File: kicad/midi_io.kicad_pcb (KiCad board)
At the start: 2 copper layers, 35.6 x 41.4 mm, 10 parts, among them J1 MIDI Out, J2 MIDI In, J3 Conn_01x04, U1 6N138

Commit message: Possible final PCB layout
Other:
- net class Default: clearance 0.0508 -> 0.1524
- rule trace_clearance: 0.0508 -> 0.1524
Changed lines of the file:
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@@
     (thickness 1.6)
     (drawings 9)
-    (tracks 52)
+    (tracks 53)
     (zones 0)
     (modules 10)
@@
     (user_trace_width 0.508)
     (user_trace_width 0.762)
-    (trace_clearance 0.0508)
+    (trace_clearance 0.1524)
     (zone_clearance 0.508)
     (zone_45_only no)
@@
     (mod_text_size 1 1)
     (mod_text_width 0.15)
-    (pad_size 4.064 4.064)
-    (pad_drill 3.048)
+    (pad_size 1.7 1.7)
+    (pad_drill 1)
     (pad_to_mask_clearance 0.0508)
     (solder_mask_min_width 0.1016)
@@
   (net 17 "Net-(U1-Pad1)")
   (net_class Default "This is the default net class."
-    (clearance 0.0508)
+    (clearance 0.1524)
     (trace_width 0.254)
     (via_dia 0.508)
@@
   (module midi_io:CUI_SDS-50J (layer F.Cu)
     (at 123.952 94.869 270)
-    (fp_text reference J2 (at -9.144 -1.778 180) (layer F.SilkS)
+    (fp_text reference J2 (at -9.144 -1.778 180) (layer F.SilkS) hide
       (effects (font (size 1.0007 1.0007) (thickness 0.1524)))
     )
@@
   (module midi_io:CUI_SDS-50J (layer F.Cu)
     (at 123.952 115.443 270)
-    (fp_text reference J1 (at -9.398 -1.524 180) (layer F.SilkS)
+    (fp_text reference J1 (at -9.398 -1.524 180) (layer F.SilkS) hide
       (effects (font (size 1.0007 1.0007) (thickness 0.1524)))
     )
@@
     (descr "Through hole straight pin header, 1x04, 2.54mm pitch, single row")
     (tags "Through hole pin header THT 1x04 2.54mm single row")
-    (fp_text reference J3 (at -0.127 10.16) (layer F.SilkS)
+    (fp_text reference J3 (at -0.127 10.16) (layer F.SilkS) hide
       (effects (font (size 1 1) (thickness 0.15)))
     )
@@
     (pad 2 thru_hole oval (at 0 2.54) (size 1.7 1.7) (drill 1) (layers *.Cu *.Mask)
       (net 1 GND))
-    (pad 1 thru_hole rect (at 0 0) (size 1.7 1.7) (drill 1) (layers *.Cu *.Mask)
+    (pad 1 thru_hole circle (at 0 0) (size 1.7 1.7) (drill 1) (layers *.Cu *.Mask)
       (net 7 VCC))
     (model ${KISYS3DMOD}/Connector_PinHeader_2.54mm.3dshapes/PinHeader_1x04_P2.54mm_Vertical.wrl
@@
   (segment (start 131.064 92.583) (end 131.826 91.821) (width 0.254) (layer F.Cu) (net 6))
   (segment (start 144.018 111.633) (end 141.478 111.633) (width 0.508) (layer B.Cu) (net 7))
-  (via (at 134.366 120.523) (size 0.508) (drill 0.254) (layers F.Cu B.Cu) (net 7))
   (segment (start 134.366 120.523) (end 132.343 120.523) (width 0.508) (layer F.Cu) (net 7))
-  (segment (start 135.89 118.999) (end 134.366 120.523) (width 0.508) (layer B.Cu) (net 7))
-  (segment (start 135.89 114.173) (end 135.89 118.999) (width 0.508) (layer B.Cu) (net 7))
+  (segment (start 135.89 118.999) (end 135.89 118.999) (width 0.508) (layer F.Cu) (net 7))
   (segment (start 141.478 111.633) (end 138.43 111.633) (width 0.508) (layer B.Cu) (net 7))
   (segment (start 138.43 111.633) (end 135.89 114.173) (width 0.508) (layer B.Cu) (net 7))
@@
   (segment (start 141.487 103.242) (end 143.002 101.727) (width 0.254) (layer F.Cu) (net 7))
   (segment (start 141.487 105.791) (end 141.487 103.242) (width 0.254) (layer F.Cu) (net 7))
+  (segment (start 135.89 114.173) (end 135.89 118.999) (width 0.508) (layer B.Cu) (net 7))
+  (segment (start 135.89 118.999) (end 134.366 120.523) (width 0.508) (layer F.Cu) (net 7))
+  (via (at 135.89 118.999) (size 0.508) (drill 0.254) (layers F.Cu B.Cu) (net 7))
   (segment (start 139.7 119.253) (end 144.018 119.253) (width 0.254) (layer F.Cu) (net 8))
   (segment (start 137.414 116.967) (end 139.7 119.253) (width 0.254) (layer F.Cu) (net 8))

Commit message: Misc
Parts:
- moved R4 20.9 mm to (160.8, 100.7)
- moved D1 20.9 mm to (159.0, 83.4)
- moved J1 20.9 mm to (144.3, 110.4)
- moved J2 20.9 mm to (144.3, 89.8)
- moved J3 20.9 mm to (164.3, 106.6)
- moved R1 20.9 mm to (151.6, 115.4)
- moved R2 20.9 mm to (151.6, 105.3)
- moved R3 20.9 mm to (151.4, 90.8)
- moved R5 20.9 mm to (151.4, 95.1)
- moved U1 20.9 mm to (163.3, 89.0)

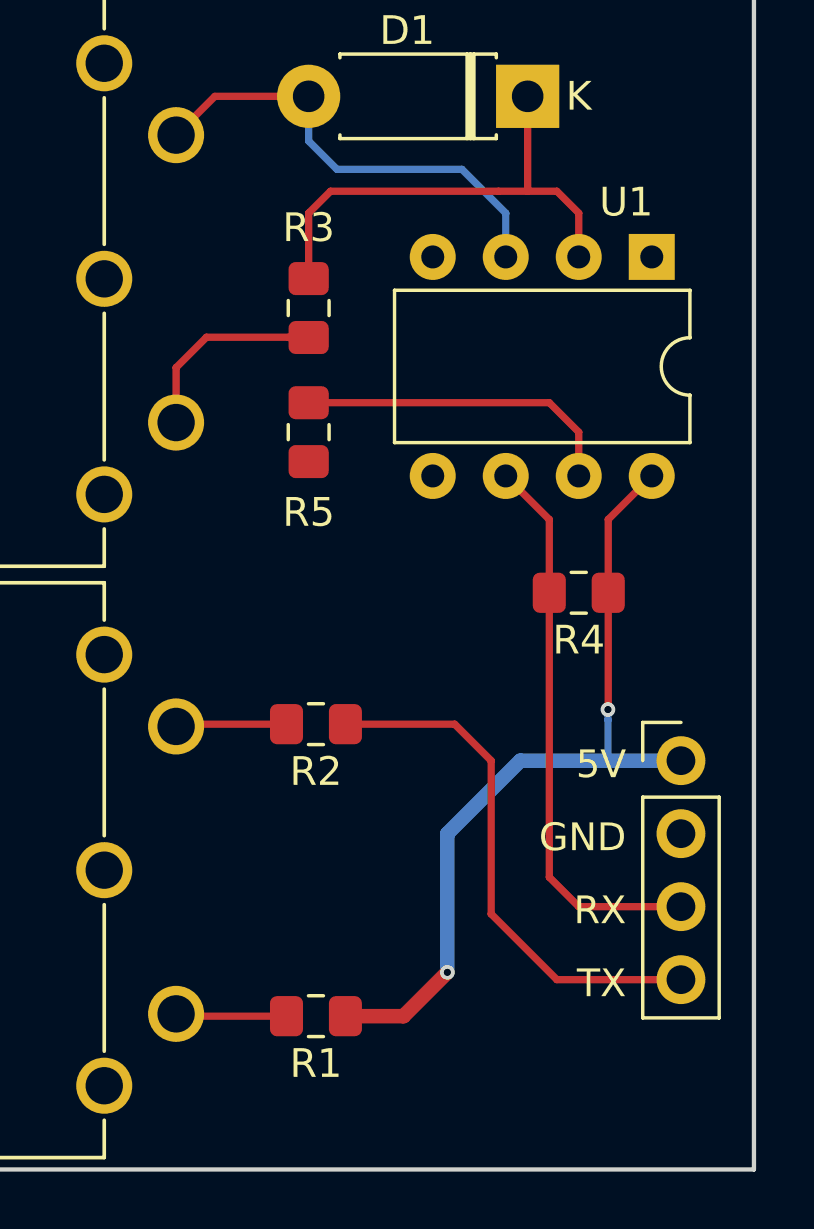
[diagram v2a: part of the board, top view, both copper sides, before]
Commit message: Update with fixes from first prototype
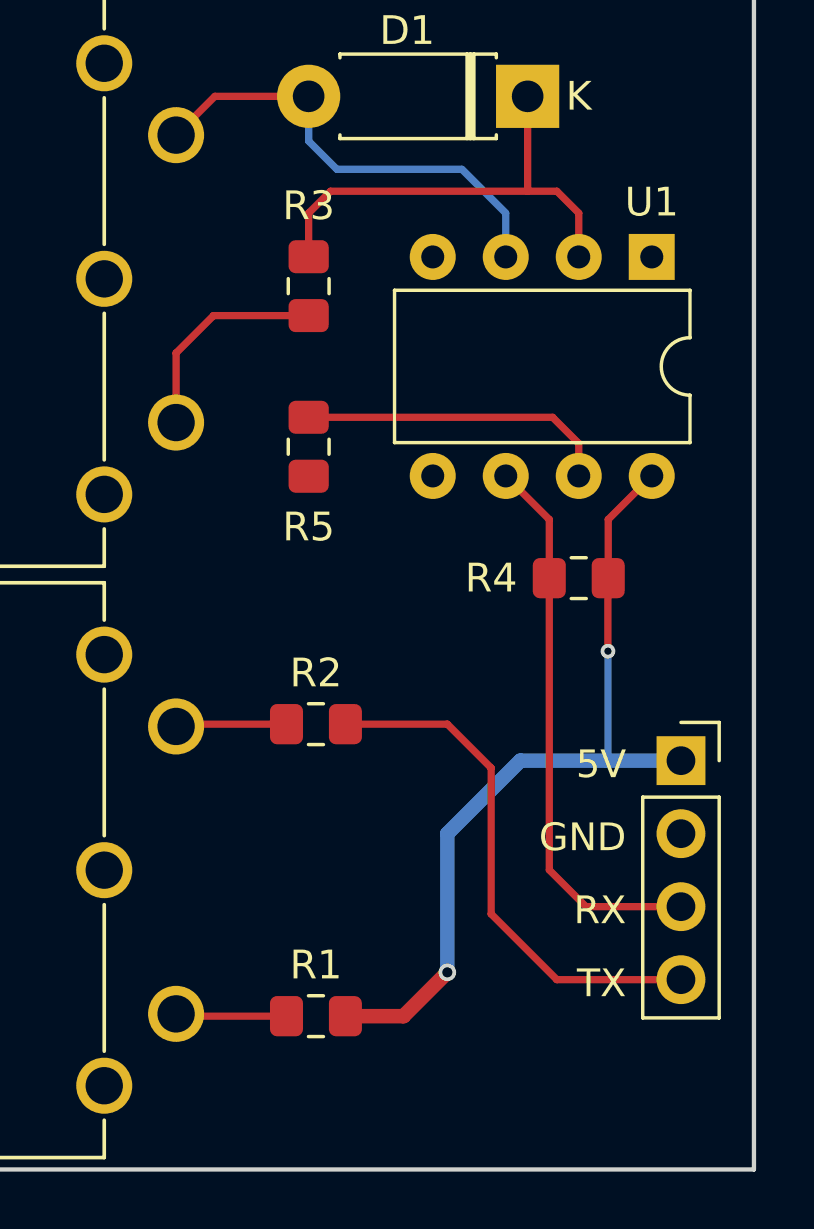
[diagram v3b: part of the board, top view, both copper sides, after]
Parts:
- J3: footprint Connector_PinHeader_2.54mm:PinHeader_1x04_P2.54mm_Vertical -> Connector_PinSocket_2.54mm:PinSocket_1x04_P2.54mm_Vertical
- moved R3 0.76 mm to (151.4, 90.0)
- moved R4 0.51 mm to (160.8, 100.2)
- moved R5 0.51 mm to (151.4, 95.6)
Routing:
- net Net-(D1-Pad1): track 17.1 -> 16.4 mm
- net Net-(J2-Pad4): track 6.97 -> 7.57 mm
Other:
- net class Default: clearance 0.1524 -> 0.254
- rule trace_clearance: 0.1524 -> 0.254
- board text added: "KUSHVIEW, LLC"

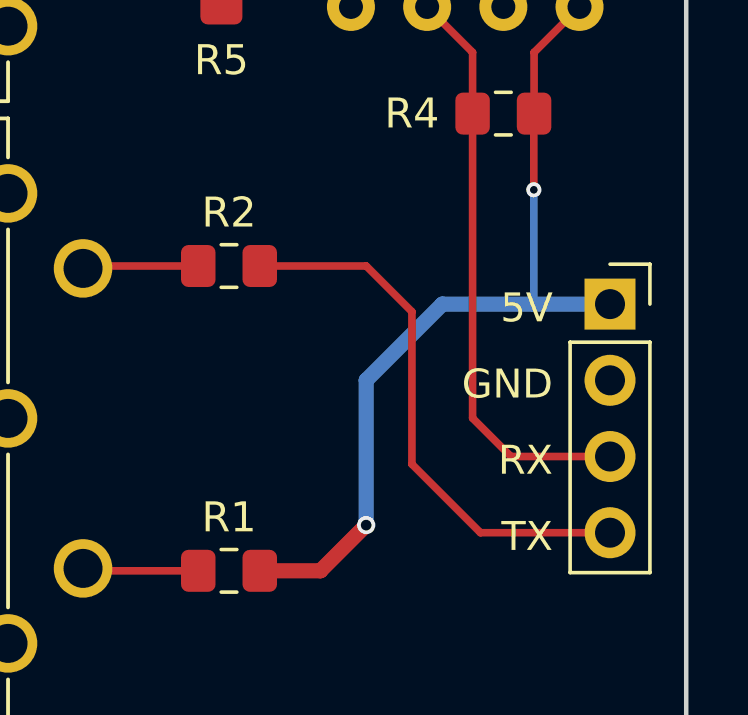
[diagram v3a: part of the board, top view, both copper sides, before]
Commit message: Use larger spacing/via sizes
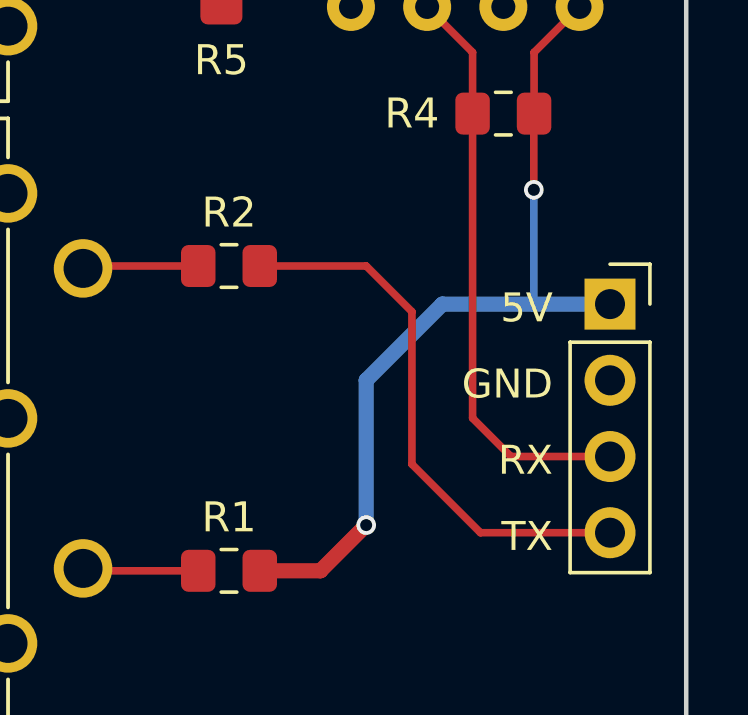
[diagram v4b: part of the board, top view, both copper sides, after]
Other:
- net class Default: via_dia 0.508 -> 0.65405; via_drill 0.254 -> 0.40005
- rule via_min_drill: 0.254 -> 0.40005
- rule via_min_size: 0.508 -> 0.65405
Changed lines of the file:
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@@
     (zone_45_only no)
     (trace_min 0.254)
-    (via_size 0.508)
-    (via_drill 0.254)
-    (via_min_size 0.508)
-    (via_min_drill 0.254)
-    (uvia_size 0.508)
-    (uvia_drill 0.254)
+    (via_size 0.65405)
+    (via_drill 0.40005)
+    (via_min_size 0.65405)
+    (via_min_drill 0.40005)
+    (user_via 0.65405 0.40005)
+    (uvia_size 0.65405)
+    (uvia_drill 0.40005)
     (uvias_allowed no)
-    (uvia_min_size 0.508)
-    (uvia_min_drill 0.254)
+    (uvia_min_size 0.65405)
+    (uvia_min_drill 0.40005)
     (edge_width 0.15)
     (segment_width 0.15)
@@
     (clearance 0.254)
     (trace_width 0.254)
-    (via_dia 0.508)
-    (via_drill 0.254)
-    (uvia_dia 0.508)
-    (uvia_drill 0.254)
+    (via_dia 0.65405)
+    (via_drill 0.40005)
+    (uvia_dia 0.65405)
+    (uvia_drill 0.40005)
     (diff_pair_width 0.254)
     (diff_pair_gap 0.25)
@@
   (segment (start 161.807 98.162) (end 163.322 96.647) (width 0.254) (layer F.Cu) (net 7))
   (segment (start 161.807 100.203) (end 161.807 98.162) (width 0.254) (layer F.Cu) (net 7))
-  (via (at 161.798 102.743) (size 0.508) (drill 0.254) (layers F.Cu B.Cu) (net 7))
+  (via (at 161.798 102.743) (size 0.65405) (drill 0.40005) (layers F.Cu B.Cu) (net 7))
   (segment (start 161.798 106.553) (end 161.798 102.743) (width 0.254) (layer B.Cu) (net 7))
   (segment (start 161.798 100.212) (end 161.807 100.203) (width 0.254) (layer F.Cu) (net 7))
@@
   (segment (start 156.21 113.919) (end 156.21 113.919) (width 0.508) (layer F.Cu) (net 7))
   (segment (start 156.21 109.093) (end 156.21 113.919) (width 0.508) (layer B.Cu) (net 7))
-  (via (at 156.21 113.919) (size 0.6096) (drill 0.3556) (layers F.Cu B.Cu) (net 7))
+  (via (at 156.21 113.919) (size 0.65405) (drill 0.40005) (layers F.Cu B.Cu) (net 7))
   (segment (start 161.798 106.553) (end 158.75 106.553) (width 0.508) (layer B.Cu) (net 7))
   (segment (start 158.75 106.553) (end 156.21 109.093) (width 0.508) (layer B.Cu) (net 7))

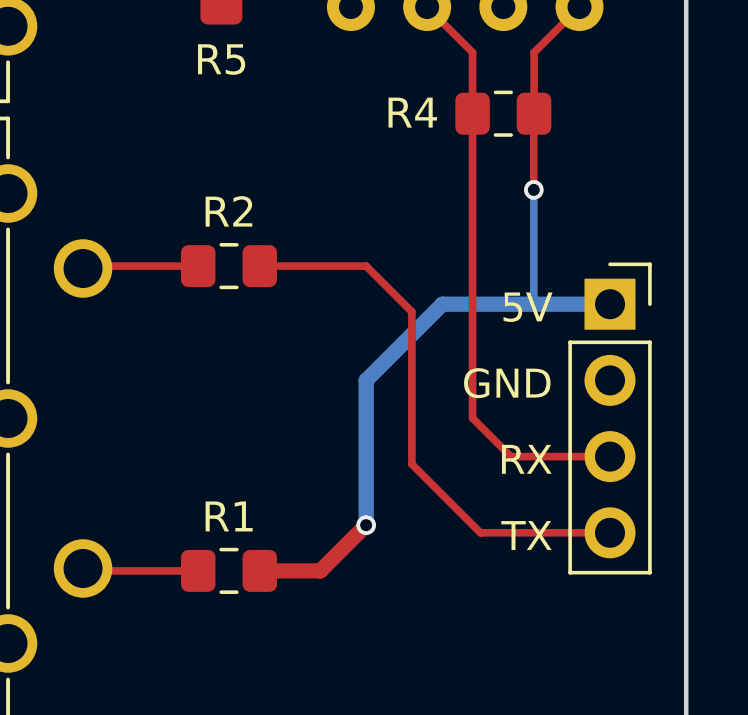
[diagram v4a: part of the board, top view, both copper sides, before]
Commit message: Updating min via sizes
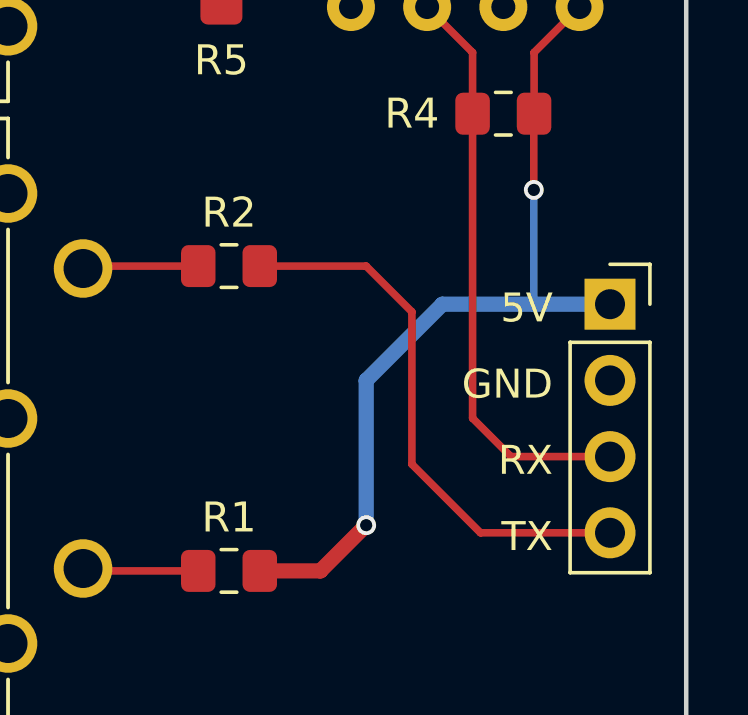
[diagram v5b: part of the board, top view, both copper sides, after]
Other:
- net class Default: via_dia 0.65405 -> 0.6604; via_drill 0.40005 -> 0.4064
- rule via_min_drill: 0.40005 -> 0.4064
- rule via_min_size: 0.65405 -> 0.6604
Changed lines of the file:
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@@
-(kicad_pcb (version 20171130) (host pcbnew "(5.1.5-0-10_14)")
+(kicad_pcb (version 20171130) (host pcbnew 5.1.5-52549c5~84~ubuntu18.04.1)
   (general
     (thickness 1.6)
@@
     (zone_45_only no)
     (trace_min 0.254)
-    (via_size 0.65405)
-    (via_drill 0.40005)
-    (via_min_size 0.65405)
-    (via_min_drill 0.40005)
-    (user_via 0.65405 0.40005)
-    (uvia_size 0.65405)
-    (uvia_drill 0.40005)
+    (via_size 0.6604)
+    (via_drill 0.4064)
+    (via_min_size 0.6604)
+    (via_min_drill 0.4064)
+    (user_via 0.6604 0.4064)
+    (uvia_size 0.6604)
+    (uvia_drill 0.4064)
     (uvias_allowed no)
-    (uvia_min_size 0.65405)
-    (uvia_min_drill 0.40005)
+    (uvia_min_size 0.6604)
+    (uvia_min_drill 0.4064)
     (edge_width 0.15)
     (segment_width 0.15)
@@
     (clearance 0.254)
     (trace_width 0.254)
-    (via_dia 0.65405)
-    (via_drill 0.40005)
-    (uvia_dia 0.65405)
-    (uvia_drill 0.40005)
+    (via_dia 0.6604)
+    (via_drill 0.4064)
+    (uvia_dia 0.6604)
+    (uvia_drill 0.4064)
     (diff_pair_width 0.254)
-    (diff_pair_gap 0.25)
+    (diff_pair_gap 0.254)
     (add_net /RX)
     (add_net /TX)
@@
   (segment (start 161.807 98.162) (end 163.322 96.647) (width 0.254) (layer F.Cu) (net 7))
   (segment (start 161.807 100.203) (end 161.807 98.162) (width 0.254) (layer F.Cu) (net 7))
-  (via (at 161.798 102.743) (size 0.65405) (drill 0.40005) (layers F.Cu B.Cu) (net 7))
+  (via (at 161.798 102.743) (size 0.6604) (drill 0.4064) (layers F.Cu B.Cu) (net 7))
   (segment (start 161.798 106.553) (end 161.798 102.743) (width 0.254) (layer B.Cu) (net 7))
   (segment (start 161.798 100.212) (end 161.807 100.203) (width 0.254) (layer F.Cu) (net 7))
@@
   (segment (start 156.21 113.919) (end 156.21 113.919) (width 0.508) (layer F.Cu) (net 7))
   (segment (start 156.21 109.093) (end 156.21 113.919) (width 0.508) (layer B.Cu) (net 7))
-  (via (at 156.21 113.919) (size 0.65405) (drill 0.40005) (layers F.Cu B.Cu) (net 7))
+  (via (at 156.21 113.919) (size 0.6604) (drill 0.4064) (layers F.Cu B.Cu) (net 7))
   (segment (start 161.798 106.553) (end 158.75 106.553) (width 0.508) (layer B.Cu) (net 7))
   (segment (start 158.75 106.553) (end 156.21 109.093) (width 0.508) (layer B.Cu) (net 7))
